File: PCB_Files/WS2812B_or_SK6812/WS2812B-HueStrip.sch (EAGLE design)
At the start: 19 parts

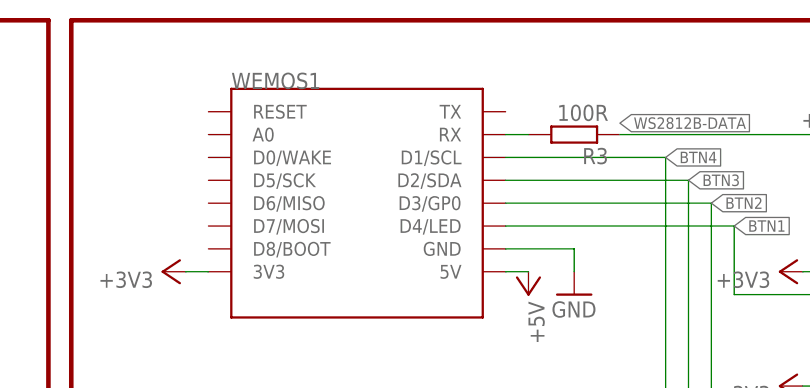
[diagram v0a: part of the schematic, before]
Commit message: Updated gerber Files to fix breaking bug
the original design had some errors that were only found after they were ordered. Those bugs hab been fixed.
Also there were new pictures exported of the design and schematic
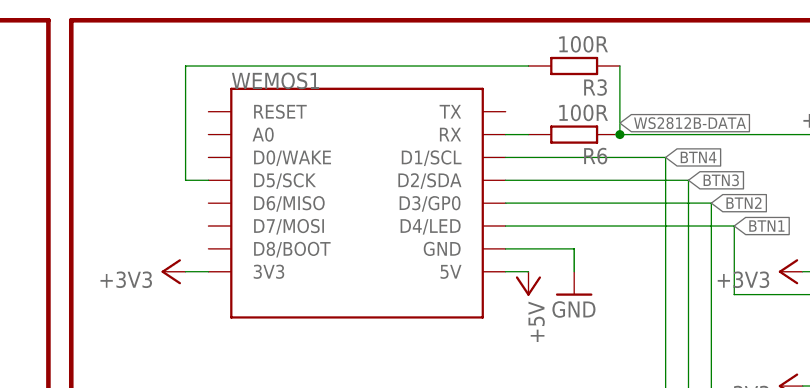
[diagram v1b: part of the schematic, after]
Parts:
- added R6: 100R, diyHue:R-EU_MULTI
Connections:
- removed net N$4: R3.2, WEMOS1.RX
- new net N$2: R3.2, WEMOS1.D5/SCK
- new net N$3: R6.2, WEMOS1.RX
- net WS2812B-DATA: now also R6.1
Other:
- moved on the sheet: R3
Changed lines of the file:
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@@
 <?xml version="1.0" encoding="utf-8"?>
 <!DOCTYPE eagle SYSTEM "eagle.dtd">
-<eagle version="9.1.3">
+<eagle version="6.6.0">
 <drawing>
 <settings>
 <setting alwaysvectorfont="yes"/>
-<setting keepoldvectorfont="yes"/>
 <setting verticaltext="up"/>
 </settings>
@@
 <part name="WEMOS1" library="esp8266modules" deviceset="WEMOS-D1-MINI" device=""/>
 <part name="POWER_IN" library="Arduino Mega 2560" deviceset="RAPC712" device="0"/>
-<part name="GND1" library="supply1" library_urn="urn:adsk.eagle:library:371" deviceset="GND" device=""/>
-<part name="P+3" library="supply1" library_urn="urn:adsk.eagle:library:371" deviceset="+5V" device=""/>
-<part name="GND2" library="supply1" library_urn="urn:adsk.eagle:library:371" deviceset="GND" device=""/>
+<part name="GND1" library="supply1" deviceset="GND" device=""/>
+<part name="P+3" library="supply1" deviceset="+5V" device=""/>
+<part name="GND2" library="supply1" deviceset="GND" device=""/>
 <part name="BTN1" library="schalter_taster" deviceset="KSM611A" device=""/>
 <part name="BTN2" library="schalter_taster" deviceset="KSM611A" device=""/>
-<part name="+3V1" library="supply1" library_urn="urn:adsk.eagle:library:371" deviceset="+3V3" device=""/>
-<part name="SJ1" library="jumper" library_urn="urn:adsk.eagle:library:252" deviceset="SJ2W" device="W" package3d_urn="urn:adsk.eagle:package:15476/1"/>
-<part name="P+1" library="supply1" library_urn="urn:adsk.eagle:library:371" deviceset="+5V" device=""/>
-<part name="P+4" library="supply1" library_urn="urn:adsk.eagle:library:371" deviceset="+12V" device=""/>
+<part name="+3V1" library="supply1" deviceset="+3V3" device=""/>
+<part name="SJ1" library="jumper" deviceset="SJ2W" device="W"/>
+<part name="P+1" library="supply1" deviceset="+5V" device=""/>
+<part name="P+4" library="supply1" deviceset="+12V" device=""/>
 <part name="R1" library="diyHue" deviceset="R-EU_MULTI" device="" value="4k7"/>
 <part name="R2" library="diyHue" deviceset="R-EU_MULTI" device="" value="4k7"/>
-<part name="GND6" library="supply1" library_urn="urn:adsk.eagle:library:371" deviceset="GND" device=""/>
-<part name="P+2" library="supply1" library_urn="urn:adsk.eagle:library:371" deviceset="+5V" device=""/>
-<part name="P+5" library="supply1" library_urn="urn:adsk.eagle:library:371" deviceset="+12V" device=""/>
+<part name="GND6" library="supply1" deviceset="GND" device=""/>
+<part name="P+2" library="supply1" deviceset="+5V" device=""/>
+<part name="P+5" library="supply1" deviceset="+12V" device=""/>
 <part name="WS2812B-PH" library="pinhead-2" deviceset="PINHD-1X03" device="_2.54-S"/>
-<part name="P+6" library="supply1" library_urn="urn:adsk.eagle:library:371" deviceset="+5V" device=""/>
-<part name="GND7" library="supply1" library_urn="urn:adsk.eagle:library:371" deviceset="GND" device=""/>
+<part name="P+6" library="supply1" deviceset="+5V" device=""/>
+<part name="GND7" library="supply1" deviceset="GND" device=""/>
 <part name="R3" library="diyHue" deviceset="R-EU_MULTI" device="" value="100R"/>
-<part name="WS2812B-WAGO" library="con-wago-508" library_urn="urn:adsk.eagle:library:196" deviceset="W237-3E" device="" package3d_urn="urn:adsk.eagle:package:10747/1"/>
-<part name="H1" library="holes" library_urn="urn:adsk.eagle:library:237" deviceset="MOUNT-PAD-ROUND" device="3.0" package3d_urn="urn:adsk.eagle:package:14280/1"/>
-<part name="H2" library="holes" library_urn="urn:adsk.eagle:library:237" deviceset="MOUNT-PAD-ROUND" device="3.0" package3d_urn="urn:adsk.eagle:package:14280/1"/>
-<part name="H3" library="holes" library_urn="urn:adsk.eagle:library:237" deviceset="MOUNT-PAD-ROUND" device="3.0" package3d_urn="urn:adsk.eagle:package:14280/1"/>
-<part name="H4" library="holes" library_urn="urn:adsk.eagle:library:237" deviceset="MOUNT-PAD-ROUND" device="3.0" package3d_urn="urn:adsk.eagle:package:14280/1"/>
-<part name="GND8" library="supply1" library_urn="urn:adsk.eagle:library:371" deviceset="GND" device=""/>
-<part name="GND9" library="supply1" library_urn="urn:adsk.eagle:library:371" deviceset="GND" device=""/>
-<part name="GND10" library="supply1" library_urn="urn:adsk.eagle:library:371" deviceset="GND" device=""/>
-<part name="GND11" library="supply1" library_urn="urn:adsk.eagle:library:371" deviceset="GND" device=""/>
+<part name="WS2812B-WAGO" library="con-wago-508" deviceset="W237-3E" device=""/>
+<part name="H1" library="holes" deviceset="MOUNT-PAD-ROUND" device="3.0"/>
+<part name="H2" library="holes" deviceset="MOUNT-PAD-ROUND" device="3.0"/>
+<part name="H3" library="holes" deviceset="MOUNT-PAD-ROUND" device="3.0"/>
+<part name="H4" library="holes" deviceset="MOUNT-PAD-ROUND" device="3.0"/>
+<part name="GND8" library="supply1" deviceset="GND" device=""/>
+<part name="GND9" library="supply1" deviceset="GND" device=""/>
+<part name="GND10" library="supply1" deviceset="GND" device=""/>
+<part name="GND11" library="supply1" deviceset="GND" device=""/>
 <part name="BTN3" library="schalter_taster" deviceset="KSM611A" device=""/>
 <part name="R4" library="diyHue" deviceset="R-EU_MULTI" device="" value="4k7"/>
 <part name="BTN4" library="schalter_taster" deviceset="KSM611A" device=""/>
 <part name="R5" library="diyHue" deviceset="R-EU_MULTI" device="" value="4k7"/>
-<part name="GND3" library="supply1" library_urn="urn:adsk.eagle:library:371" deviceset="GND" device=""/>
-<part name="GND4" library="supply1" library_urn="urn:adsk.eagle:library:371" deviceset="GND" device=""/>
-<part name="GND5" library="supply1" library_urn="urn:adsk.eagle:library:371" deviceset="GND" device=""/>
-<part name="GND12" library="supply1" library_urn="urn:adsk.eagle:library:371" deviceset="GND" device=""/>
-<part name="+3V2" library="supply1" library_urn="urn:adsk.eagle:library:371" deviceset="+3V3" device=""/>
-<part name="+3V3" library="supply1" library_urn="urn:adsk.eagle:library:371" deviceset="+3V3" device=""/>
-<part name="+3V4" library="supply1" library_urn="urn:adsk.eagle:library:371" deviceset="+3V3" device=""/>
-<part name="+3V5" library="supply1" library_urn="urn:adsk.eagle:library:371" deviceset="+3V3" device=""/>
+<part name="GND3" library="supply1" deviceset="GND" device=""/>
+<part name="GND4" library="supply1" deviceset="GND" device=""/>
+<part name="GND5" library="supply1" deviceset="GND" device=""/>
+<part name="GND12" library="supply1" deviceset="GND" device=""/>
+<part name="+3V2" library="supply1" deviceset="+3V3" device=""/>
+<part name="+3V3" library="supply1" deviceset="+3V3" device=""/>
+<part name="+3V4" library="supply1" deviceset="+3V3" device=""/>
+<part name="+3V5" library="supply1" deviceset="+3V3" device=""/>
 <part name="U$1" library="diyHue" deviceset="BUCK_CONVERTER_TE818" device=""/>
+<part name="R6" library="diyHue" deviceset="R-EU_MULTI" device="" value="100R"/>
 </parts>
 <sheets>
@@
 </instance>
 <instance part="GND7" gate="1" x="142.24" y="45.72" rot="R270"/>
-<instance part="R3" gate="G$1" x="111.76" y="48.26" rot="R180"/>
+<instance part="R3" gate="G$1" x="111.76" y="55.88" rot="R180"/>
 <instance part="WS2812B-WAGO" gate="-1" x="162.56" y="45.72" rot="R180"/>
 <instance part="WS2812B-WAGO" gate="-2" x="162.56" y="48.26" rot="R180"/>
@@
 </instance>
 <instance part="U$1" gate="G$1" x="15.24" y="15.24"/>
+<instance part="R6" gate="G$1" x="111.76" y="48.26" rot="R180"/>
 </instances>
 <busses>
@@
 <pinref part="R3" gate="G$1" pin="1"/>
 <wire x1="149.86" y1="48.26" x2="116.84" y2="48.26" width="0.1524" layer="91"/>
+<wire x1="116.84" y1="48.26" x2="116.84" y2="55.88" width="0.1524" layer="91"/>
 <label x="116.84" y="49.53" size="1.27" layer="95" xref="yes"/>
 <pinref part="WS2812B-WAGO" gate="-2" pin="KL"/>
 <wire x1="149.86" y1="48.26" x2="157.48" y2="48.26" width="0.1524" layer="91"/>
 <junction x="149.86" y="48.26"/>
-</segment>
-</net>
-<net name="N$4" class="0">
-<segment>
-<pinref part="WEMOS1" gate="D1" pin="RX"/>
-<pinref part="R3" gate="G$1" pin="2"/>
-<wire x1="106.68" y1="48.26" x2="104.14" y2="48.26" width="0.1524" layer="91"/>
+<pinref part="R6" gate="G$1" pin="1"/>
+<junction x="116.84" y="48.26"/>
 </segment>
 </net>
@@
 </segment>
 </net>
+<net name="N$2" class="0">
+<segment>
+<pinref part="WEMOS1" gate="D1" pin="D5/SCK"/>
+<wire x1="71.12" y1="43.18" x2="68.58" y2="43.18" width="0.1524" layer="91"/>
+<wire x1="68.58" y1="43.18" x2="68.58" y2="55.88" width="0.1524" layer="91"/>
+<wire x1="68.58" y1="55.88" x2="106.68" y2="55.88" width="0.1524" layer="91"/>
+<pinref part="R3" gate="G$1" pin="2"/>
+</segment>
+</net>
+<net name="N$3" class="0">
+<segment>
+<pinref part="WEMOS1" gate="D1" pin="RX"/>
+<pinref part="R6" gate="G$1" pin="2"/>
+<wire x1="104.14" y1="48.26" x2="106.68" y2="48.26" width="0.1524" layer="91"/>
+</segment>
+</net>
 </nets>
 </sheet>
@@
 which will not be processed correctly with this version.
 </note>
-<note version="8.2" severity="warning">
-Since Version 8.2, EAGLE supports online libraries. The ids
-of those online libraries will not be understood (or retained)
-with this version.
-</note>
-<note version="8.3" severity="warning">
-Since Version 8.3, EAGLE supports URNs for individual library
-assets (packages, symbols, and devices). The URNs of those assets
-will not be understood (or retained) with this version.
-</note>
-<note version="8.3" severity="warning">
-Since Version 8.3, EAGLE supports the association of 3D packages
-with devices in libraries, schematics, and board files. Those 3D
-packages will not be understood (or retained) with this version.
-</note>
 </compatibility>
